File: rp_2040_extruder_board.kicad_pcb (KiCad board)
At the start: 2 copper layers, 70 parts, among them J1 Conn_01x04, J10 Screw_Terminal_01x02, J11 Screw_Terminal_01x02, J12 Screw_Terminal_01x02, J13 Conn_01x02, J14 Screw_Terminal_01x02, J15 Conn_01x02, J16 Conn_01x02, J17 USB_C_Receptacle, J18 Conn_ARM_SWD_TagConnect_TC2030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

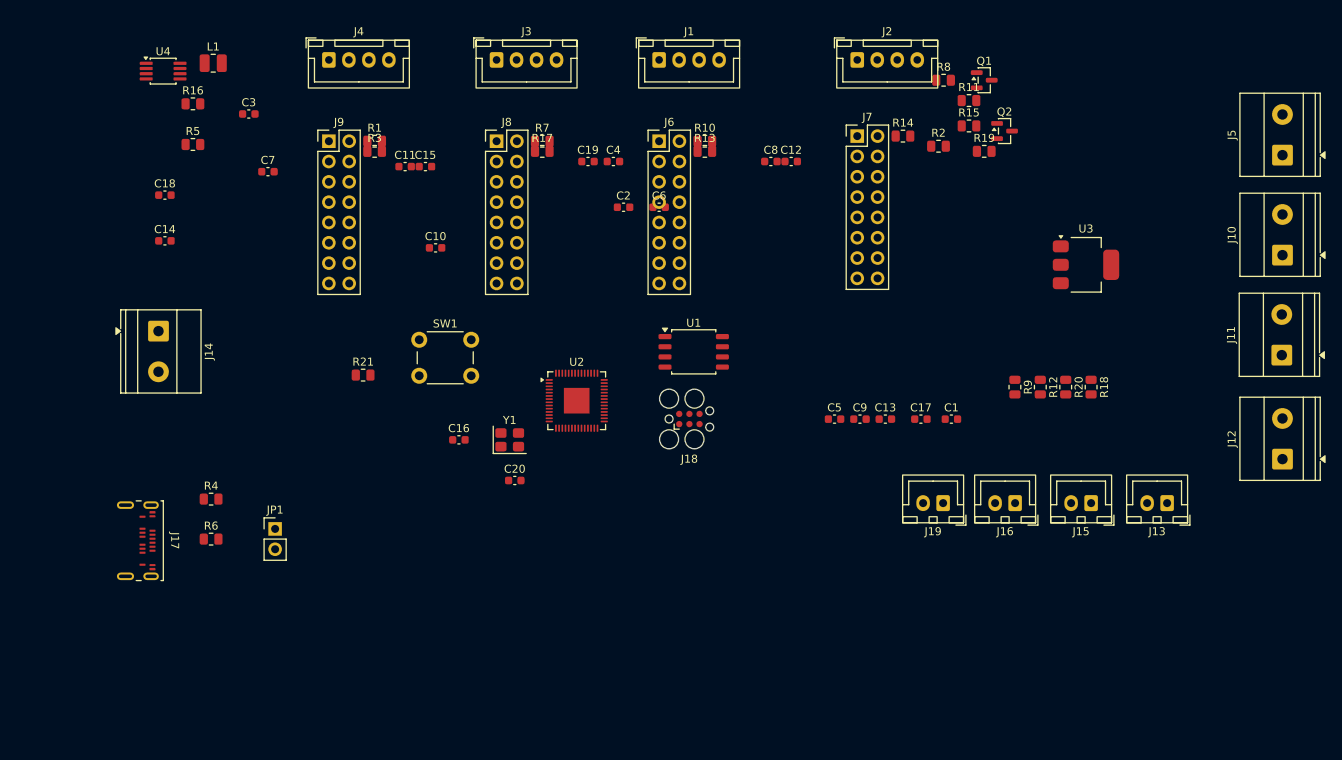
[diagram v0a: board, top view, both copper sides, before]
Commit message: more compact
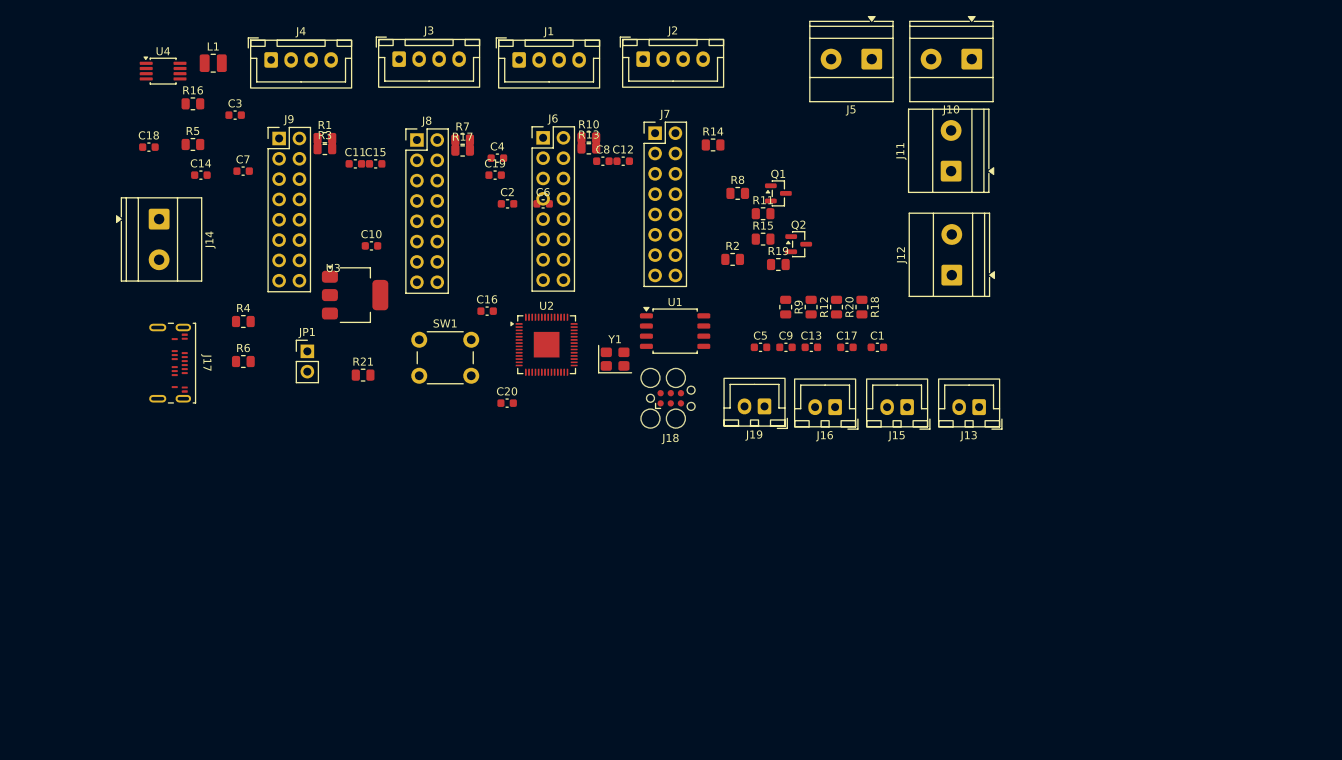
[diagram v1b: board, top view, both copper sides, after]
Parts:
- moved U3 91.4 mm to (42.5, 45.5)
- moved J5 52.7 mm to (107.1, 16.0), turned to 180 degrees
- moved J11 47.3 mm to (117.0, 30.0)
- moved J12 47.3 mm to (117.1, 43.0)
- moved J10 45.9 mm to (119.6, 16.0), turned to 180 degrees
- moved R12 30.3 mm to (99.5, 47.0)
- moved R18 30.3 mm to (105.8, 47.0)
- moved R20 30.3 mm to (102.7, 47.0)
- moved R9 30.3 mm to (96.3, 47.0)
- moved Q2 29.4 mm to (97.9, 39.1)
- moved Q1 29.4 mm to (95.4, 32.8)
- moved R11 29.4 mm to (93.5, 35.3)
- moved R15 29.4 mm to (93.5, 38.5)
- moved R19 29.4 mm to (95.4, 41.7)
- moved R2 29.4 mm to (89.7, 41.0)
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
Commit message: even more compact
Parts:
- moved J10 62.9 mm to (94.0, 73.5), turned to 90 degrees
- moved J11 59.7 mm to (94.0, 85.0)
- moved J12 58.3 mm to (94.0, 96.5)
- moved J13 57.1 mm to (77.5, 97.0)
- moved J15 57.1 mm to (68.5, 97.0)
- moved J16 57.1 mm to (59.5, 97.0)
- moved J19 57.1 mm to (50.7, 96.9)
- moved C13 49.4 mm to (62.8, 85.0)
- moved C5 49.4 mm to (56.4, 85.0)
- moved C9 49.4 mm to (59.6, 85.0)
- moved C1 49.4 mm to (71.0, 85.0)
- moved C17 49.4 mm to (67.2, 85.0)
- moved J5 47.8 mm to (94.0, 62.0), turned to 90 degrees
- moved R12 45.9 mm to (63.5, 75.5)
- moved R18 45.9 mm to (69.8, 75.5)
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
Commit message: Added some tracks
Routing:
- net /5V_MAIN: track 0.00 -> 62.5 mm
- net GND: track 0.00 -> 60.8 mm
- net /VBUS_USB: track 0.00 -> 18.1 mm
- net Net-(J5-CC2): track 0.00 -> 10.5 mm
- net Net-(J11-~{RESET}): track 0.00 -> 3.42 mm
